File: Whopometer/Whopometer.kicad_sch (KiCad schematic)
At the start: 1 part, among them U1 H3LIS331DLTR

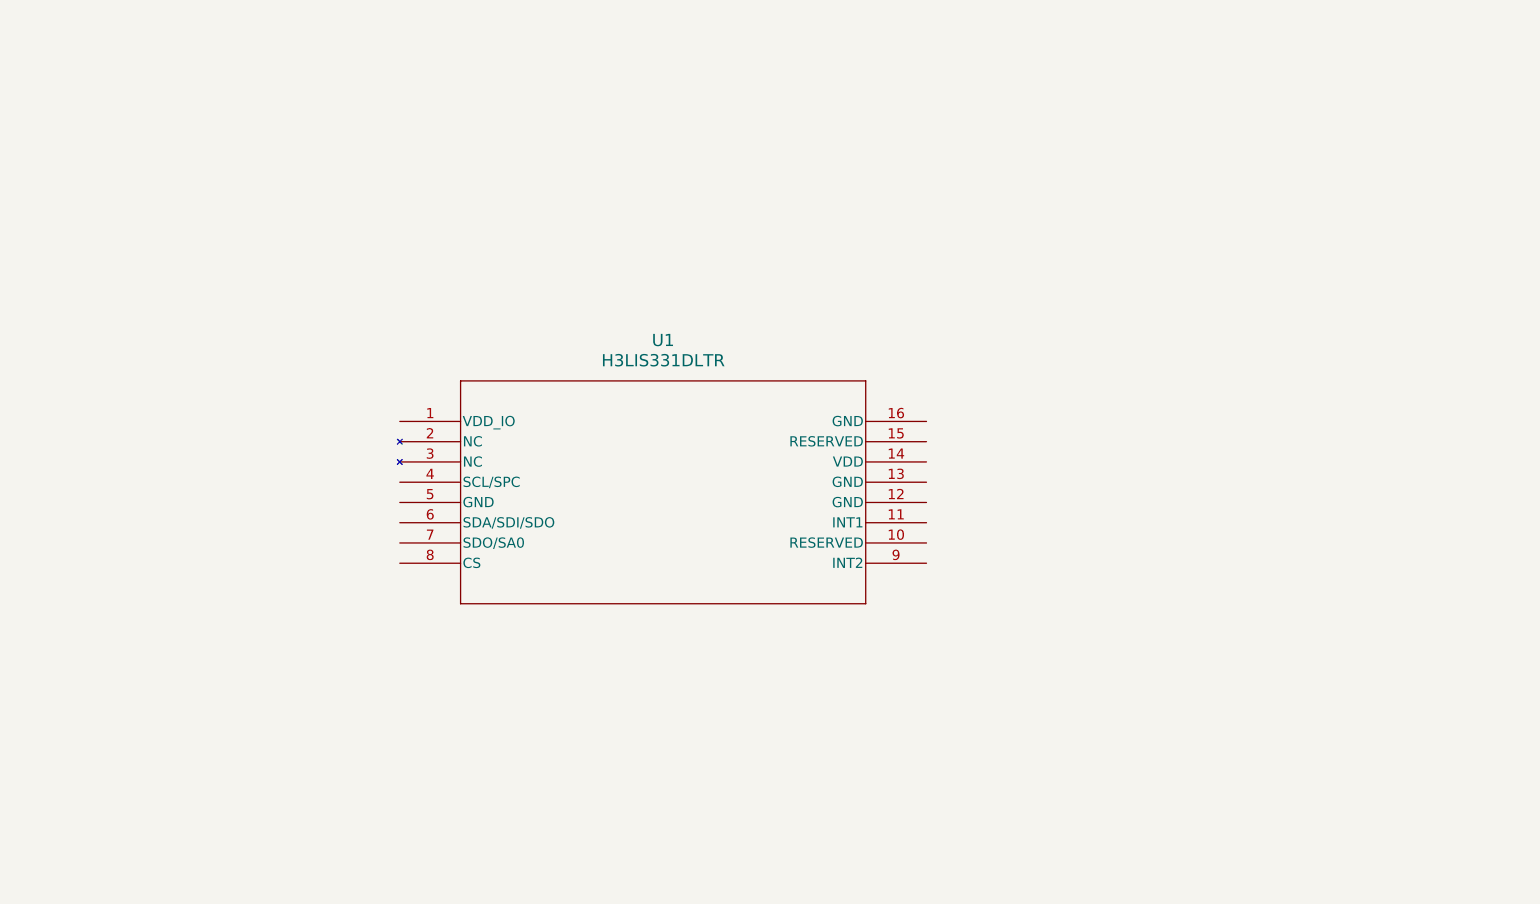
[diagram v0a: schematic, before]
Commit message: started stm32 schematic
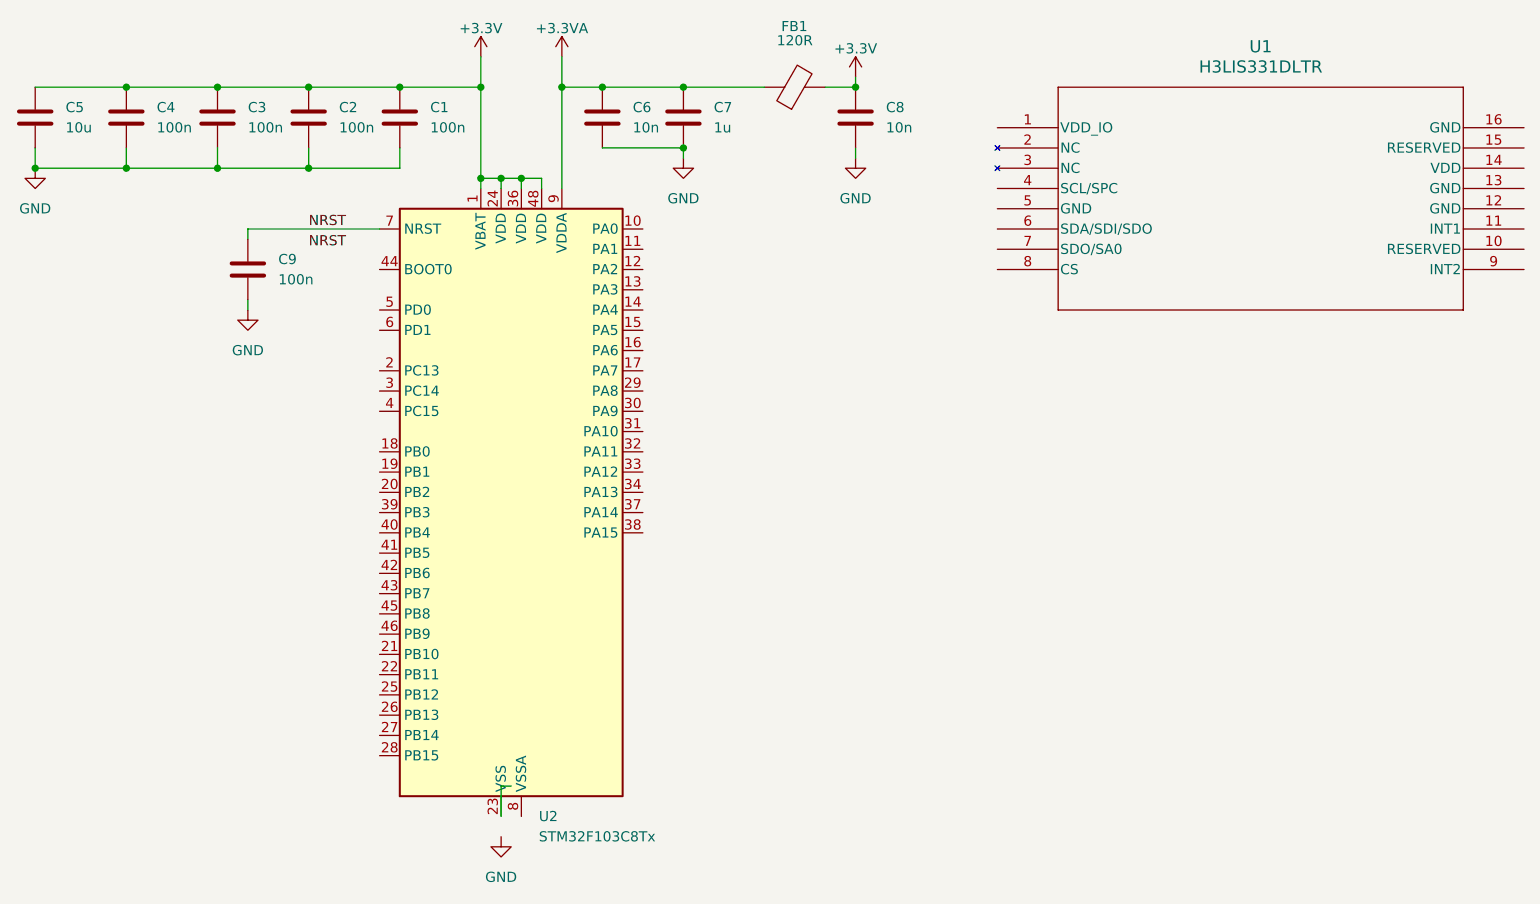
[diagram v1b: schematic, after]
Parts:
- added C1, C2, C3, C4, C9: 100n, symbol Device:C
- added C5: 10u, symbol Device:C
- added C6, C8: 10n, symbol Device:C
- added C7: 1u, symbol Device:C
- added FB1: 120R, symbol Device:FerriteBead
- added U2: STM32F103C8Tx, Package_QFP:LQFP-48_7x7mm_P0.5mm, symbol MCU_ST_STM32F1:STM32F103C8Tx
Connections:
- new net: U2.23 (VSS), U2.35 (VSS), U2.47 (VSS)
- new net +3.3V: C1.1, C2.1, C3.1, C4.1, C5.1, C8.1, FB1.2, U2.1 (VBAT), U2.24 (VDD), U2.36 (VDD), U2.48 (VDD)
- new net +3.3VA: C6.1, C7.1, FB1.1, U2.9 (VDDA)
- new net GND: C1.2, C2.2, C3.2, C4.2, C5.2, C6.2, C7.2, C8.2, C9.2
- new net NRST: C9.1, U2.7 (NRST)
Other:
- moved on the sheet: U1

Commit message: STM 32 time
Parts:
- added C10, C11: 10p, symbol Device:C
- added C12, C13: 22u, symbol Device:C
- added D1: RED, symbol Device:LED
- added J1: USB_B_Micro, symbol Connector:USB_B_Micro
- added J2: Conn_01x04_Socket, symbol Connector:Conn_01x04_Socket
- added J3: Micro_SD_Card, symbol Connector:Micro_SD_Card
- added R1: 10k, symbol Device:R
- added R2, R3: 1.5k, symbol Device:R
- added SW1: SW_SPDT, symbol Switch:SW_SPDT
- added U3: AMS1117-3.3, Package_TO_SOT_SMD:SOT-223-3_TabPin2, symbol Regulator_Linear:AMS1117-3.3
- added Y1: 16MHz, symbol Device:Crystal_GND24
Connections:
- net GND is gone; now on net +3.3VA: C1.2, C2.2, C3.2, C4.2, C5.2, C6.2, C7.2, C8.2, C9.2
- net +3.3V: now also C13.1, D1.2 (A), J2.1 (Pin_1), R2.1, SW1.3 (C), U3.2 (VO)
- net +3.3VA: now also U2.23 (VSS), U2.35 (VSS), U2.47 (VSS), U2.8 (VSSA), C10.2, C11.2, C12.2, C13.2, J1.5 (GND), J2.4 (Pin_4), R3.2, SW1.1 (A), U3.1 (GND), Y1.2, Y1.4
- net SPI1_CS: now reaches U2.14 (PA4)
- net SPI1_SCK: now reaches U2.15 (PA5)
- net SPI1_MISO: now reaches U2.16 (PA6)
- net SPI1_MOSI: now reaches U2.17 (PA7)
- net SPI2_CS: now reaches U2.25 (PB12)
- net SPI2_SCK: now reaches U2.26 (PB13)
- net SPI2_MISO: now reaches U2.27 (PB14)
- net SPI2_MOSI: now reaches U2.28 (PB15)
- net USB_D-: now reaches U2.32 (PA11)
- net USB_D-: now also J1.2 (D-)
- net USB_D+: now reaches U2.33 (PA12)
- net USB_D+: now also J1.3 (D+), R2.2
- net SWDIO: now reaches U2.34 (PA13)
- net SWDIO: now also J2.2 (Pin_2)
- net SWCLCK: now reaches U2.37 (PA14)
- net SWCLCK: now also J2.3 (Pin_3)
- net I2C1_SCL: now reaches U2.42 (PB6)
- net I2C1_SDA: now reaches U2.43 (PB7)
- net BOOT0: now reaches U2.44 (BOOT0)
- net BOOT0: now also R1.2
- net HSE_IN: now reaches U2.5 (PD0)
- net HSE_IN: now also C10.1, Y1.1
- net HSE_OUT: now reaches U2.6 (PD1)
- net HSE_OUT: now also C11.1, Y1.3
- new net P_LED_K: D1.1 (K), R3.1
- new net SW_BOOT0: R1.1, SW1.2 (B)
- new net VBUS: C12.1, J1.1 (VBUS), U3.3 (VI)
- no-connect marks 0 -> 2
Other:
- moved on the sheet: C9, U1

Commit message: Yuppers
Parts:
- added C14, C17: 10u, Capacitor_SMD:C_0201_0603Metric, symbol Device:C
- added C15, C16, C18: 100n, Capacitor_SMD:C_0201_0603Metric, symbol Device:C
- added H1, H2, H3, H4, H5, H6, H7, H8: MountingHole, MountingHole:MountingHole_2.2mm_M2_ISO7380_Pad, symbol Mechanical:MountingHole
- added J4: Conn_01x02_Socket, Connector_PinHeader_2.00mm:PinHeader_1x02_P2.00mm_Horizontal, symbol Connector:Conn_01x02_Socket
- added R10, R11, R12, R8, R9: 10k, Resistor_SMD:R_0603_1608Metric, symbol Device:R
- added R4, R5, R6, R7: 4.7k, Resistor_SMD:R_0603_1608Metric, symbol Device:R
- added U4: W25Q128JVS, Package_SO:SOIC-8_5.23x5.23mm_P1.27mm, symbol Memory_Flash:W25Q128JVS
- C1, C10, C11, C12, C13, C2, C3, C4, C5, C6, C7, C8, C9: footprint (none) -> Capacitor_SMD:C_0201_0603Metric
- D1: footprint (none) -> LED_SMD:LED_0805_2012Metric
- FB1: footprint (none) -> Inductor_SMD:L_0805_2012Metric
- J1: footprint (none) -> Connector_USB:USB_Micro-B_Amphenol_10104110_Horizontal
- J2: footprint (none) -> Connector_PinHeader_2.00mm:PinHeader_1x04_P2.00mm_Horizontal
- J3: footprint (none) -> Connector_Card:microSD_HC_Molex_104031-0811
- R1, R2, R3: footprint (none) -> Resistor_SMD:R_0603_1608Metric
- SW1: footprint (none) -> Button_Switch_SMD:SW_SPDT_PCM12
- U1: footprint QFN_31DLTR_STM -> footprints:QFN_31DLTR_STM
- Y1: footprint (none) -> Crystal:Crystal_SMD_3225-4Pin_3.2x2.5mm
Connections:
- net +3.3V: now also J3.4 (VDD), U1.1 (VDD_IO), U1.14 (VDD), U1.15 (RESERVED), U1.8 (CS), C14.1, C15.1, C16.1, C17.1, C18.1, R10.2, R11.1, R12.1, R4.1, R5.1, R6.1, R7.1, R8.2, R9.2, U4.3 (IO2), U4.7 (IO3), U4.8 (VCC)
- net +3.3VA: no longer C1.2, C10.2, C11.2, C12.2, C13.2, C2.2, C3.2, C4.2, C5.2, C6.2, C7.2, C8.2, C9.2, J1.5 (GND), J2.4 (Pin_4), R3.2, SW1.1 (A), U2.23 (VSS), U2.35 (VSS), U2.47 (VSS), U2.8 (VSSA), U3.1 (GND), Y1.2, Y1.4
- net I2C1_SCL: now also U1.4 (SCL/SPC), R5.2
- net I2C1_SDA: now also U1.6 (SDA/SDI/SDO), R4.2
- net SPI1_CS: now also J3.2 (DAT3/CD), R7.2
- net SPI1_MISO: now also J3.7 (DAT0), R9.1
- net SPI1_MOSI: now also J3.3 (CMD), R12.2
- net SPI1_SCK: now also J3.5 (CLK), R8.1
- net SPI2_CS: now also R6.2, U4.1 (~{CS})
- net SPI2_MISO: now also U4.2 (DO(IO1))
- net SPI2_MOSI: now also U4.5 (DI(IO0))
- net SPI2_SCK: now also U4.6 (CLK)
- net VBUS: now also J4.1 (Pin_1)
- net INT_1: now reaches U2.40 (PB4)
- net INT_1: now also U1.11 (INT1)
- net INT_2: now reaches U2.41 (PB5)
- net INT_2: now also U1.9 (INT2)
- net at J3.1 (DAT2): now also R11.2
- net GND: now reaches J3.6 (VSS)
- net GND: now also C1.2, C10.2, C11.2, C12.2, C13.2, C2.2, C3.2, C4.2, C5.2, C6.2, C7.2, C8.2, C9.2, J1.5 (GND), J2.4 (Pin_4), R3.2, SW1.1 (A), U1.10 (RESERVED), U1.12 (GND), U1.13 (GND), U1.16 (GND), U1.5 (GND), U1.7 (SDO/SA0), U2.23 (VSS), U2.35 (VSS), U2.47 (VSS), U2.8 (VSSA), U3.1 (GND), Y1.2, Y1.4, C14.2, C15.2, C16.2, C17.2, C18.2, J4.2 (Pin_2), U4.4 (GND)
- net at J3.8 (DAT1): now also R10.1
- no-connect marks 2 -> 5
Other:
- moved on the sheet: J3, U1

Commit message: pls
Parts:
- removed H3, H4, H5, H6, H7, H8: MountingHole, MountingHole:MountingHole_2.2mm_M2_ISO7380_Pad, symbol Mechanical:MountingHole
- added C21, C23: 0.1u, Capacitor_SMD:C_0201_0603Metric, symbol Device:C
- added C22: 2200pF, Capacitor_SMD:C_0201_0603Metric, symbol Device:C
- added C24: 0.01uF, Capacitor_SMD:C_0201_0603Metric, symbol Device:C
- added U6: MPU-6050, Sensor_Motion:InvenSense_QFN-24_4x4mm_P0.5mm, symbol Sensor_Motion:MPU-6050
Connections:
- net +3.3V: now also C23.2, C24.1, U6.13 (VDD), U6.8 (VLOGIC)
- net GND: now also C21.1, C22.2, C23.1, C24.2, U6.1 (CLKIN), U6.11 (FSYNC), U6.18 (GND), U6.9 (AD0)
- net SWCLCK: now also J2.2 (Pin_2); no longer J2.3 (Pin_3)
- net SWDIO: now also J2.3 (Pin_3); no longer J2.2 (Pin_2)
- net INT_3: now reaches U2.20 (PB2)
- net INT_3: now also U6.12 (INT)
- net I2C2_SCL: now reaches U2.21 (PB10)
- net I2C2_SCL: now also U6.23 (SCL)
- net I2C2_SDA: now reaches U2.22 (PB11)
- net I2C2_SDA: now also U6.24 (SDA)
- new net: C21.2, U6.10 (REGOUT)
- new net: C22.1, U6.20 (CPOUT)
- no-connect marks 5 -> 7
